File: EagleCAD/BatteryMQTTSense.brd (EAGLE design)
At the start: 43 x 21 mm, 10 parts

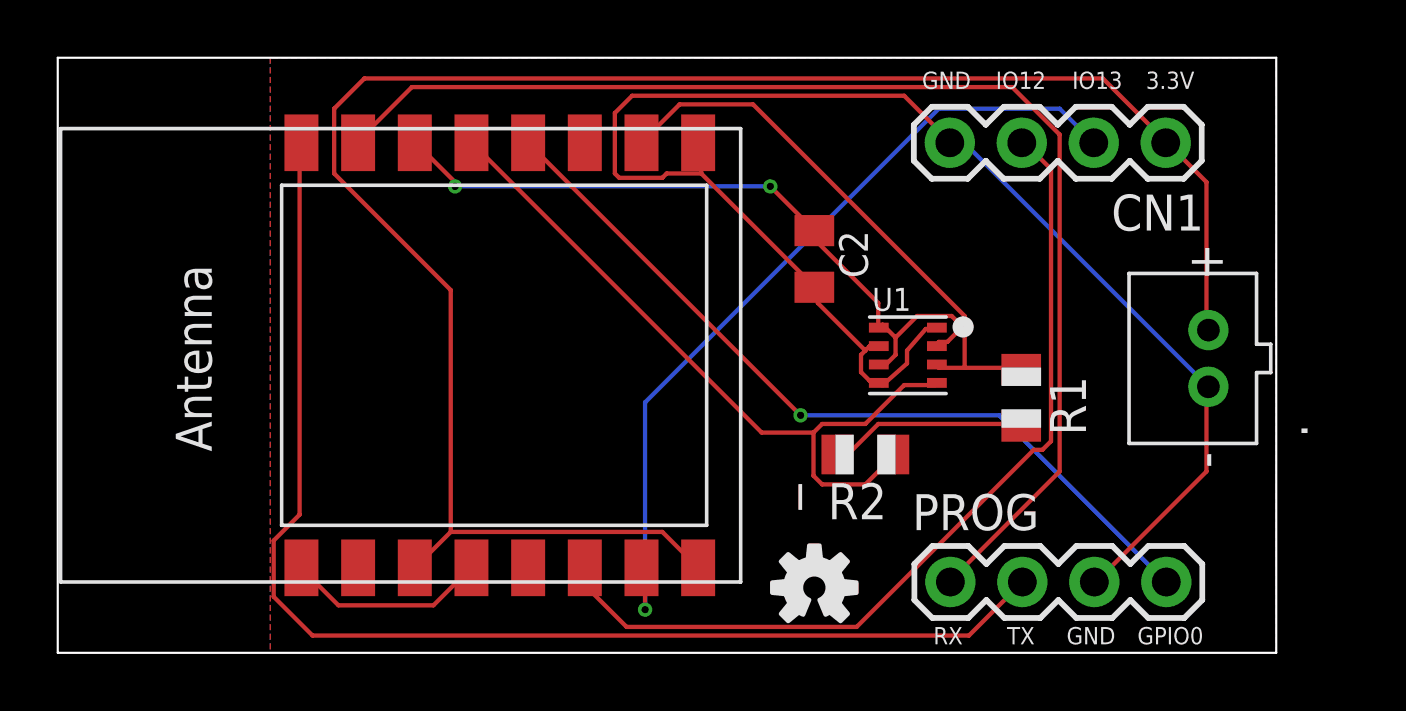
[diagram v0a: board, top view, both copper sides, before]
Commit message: adding new design for eaglecad files, using daughterboard for bme
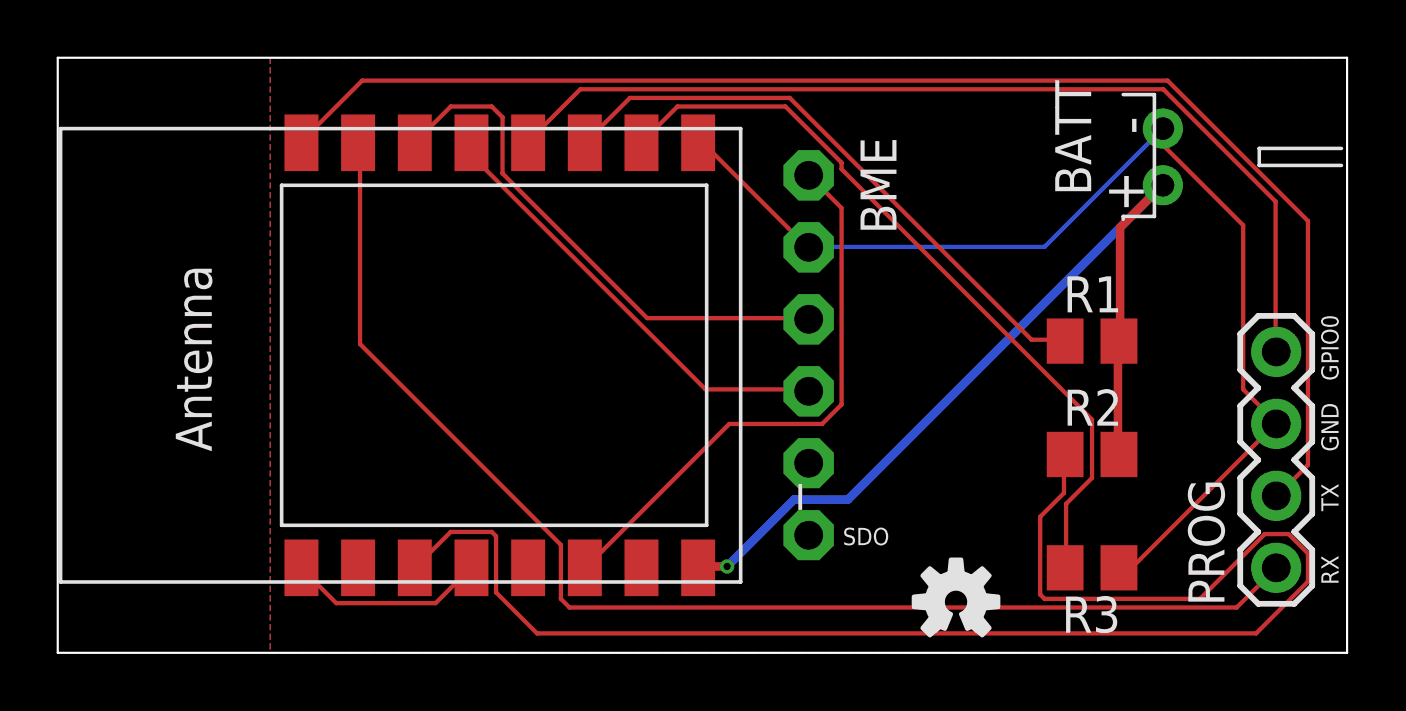
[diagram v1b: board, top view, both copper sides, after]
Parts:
- removed .: (no value), adafruit:JST-PH-2-THM
- removed C2: (no value), adafruit:C0805K
- removed CN1: (no value), adafruit:1X04-BIG
- removed U1: (no value), Adafruit BME280:MICROBUILDER_BME280
- added BATT: (no value), adafruit:JST-PH-2-THM-RA
- added BME: (no value), adafruit:1X06-CLEANBIG
- added R3: (no value), adafruit:M0805
- R1, R2: device adafruit:R0805 -> adafruit:M0805
- moved FRAME1 11.5 mm to (11.0, -3.50)
- moved PROG 11.5 mm to (43.0, 3.00), turned to 90 degrees
- moved R2 8.00 mm to (36.5, 7.00), turned to 0 degrees
- moved LOGO1 5.02 mm to (31.7, 1.80)
- moved R1 3.20 mm to (36.5, 11.0), turned to 0 degrees
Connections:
- removed net CSB_VDDIO: R1.2, R2.2
- removed net GPIO12: CN1.3, _.6
- new net CH_PD: R2.1, _.3
- new net CSB: BME.5
- new net GPIO15: R3.2, _.10
- new net SDO: BME.6
- net 3.3V: now also BATT.1, R1.2, R2.2; no longer ..1, CN1.1, _.3
- net ESP_PWR: now also BME.1, _.6; no longer C2.1, U1.2, U1.6, U1.8, _.14
- net GND: now also BATT.2, BME.2, R3.1; no longer ..2, C2.2, CN1.4, U1.1, U1.5, U1.7
- net GPIO13: no longer CN1.2
- net GPIO2: now also R1.1
- net SCL: now also BME.3, _.14; no longer R2.1, U1.4, _.13
- net SDA: now also BME.4, _.13; no longer R1.1, U1.3, _.10
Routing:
- net CH_PD: track 0.00 -> 52.5 mm
- net 3.3V: track 65.7 -> 32.2 mm, vias 0 -> 1
- net GPIO12: track 31.8 -> 0.00 mm
- net GPIO13: track 29.5 -> 0.00 mm, vias 1 -> 0
- net GPIO15: track 0.00 -> 26.8 mm
- net GPIO2: track 0.00 -> 21.2 mm
- net GND: track 54.5 -> 39.4 mm
- net SCL: track 26.3 -> 18.7 mm
- net CSB_VDDIO: track 7.01 -> 0.00 mm
- net ESP_PWR: track 25.8 -> 20.0 mm, vias 2 -> 0
- net GPIO0: track 28.9 -> 34.1 mm, vias 1 -> 0
- net TX: track 44.2 -> 48.7 mm
- net SDA: track 20.0 -> 15.8 mm
- net RX: track 43.7 -> 45.0 mm
- added copper zone on layer 16, net GN
- removed copper zone on layer 16, net GND
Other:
- board size 43 x 21 mm -> 45.5 x 21 mm
- board text added: "SDO"
- board text added: "v1.2"
- board text removed: "3.3V"
- board text removed: "IO12"
- board text removed: "IO13"
- board text removed: "v1.0"
